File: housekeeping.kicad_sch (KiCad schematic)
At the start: 42 parts, among them U13 DAC53401, U15 MC34063A, U16 MC34063A

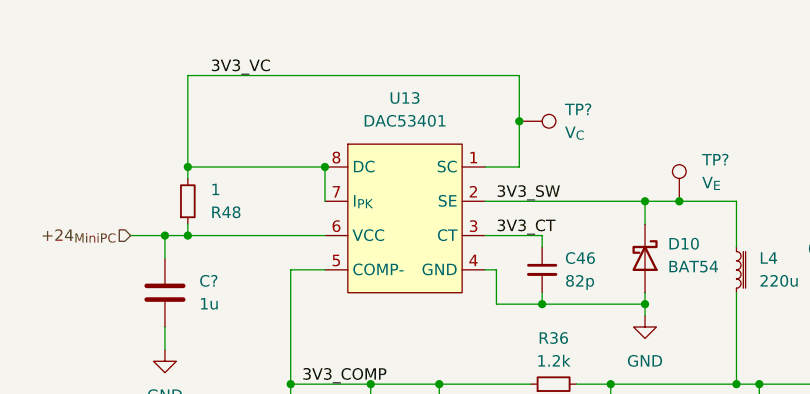
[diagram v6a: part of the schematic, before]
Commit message: Find suitable op-amp for buffer in current sense
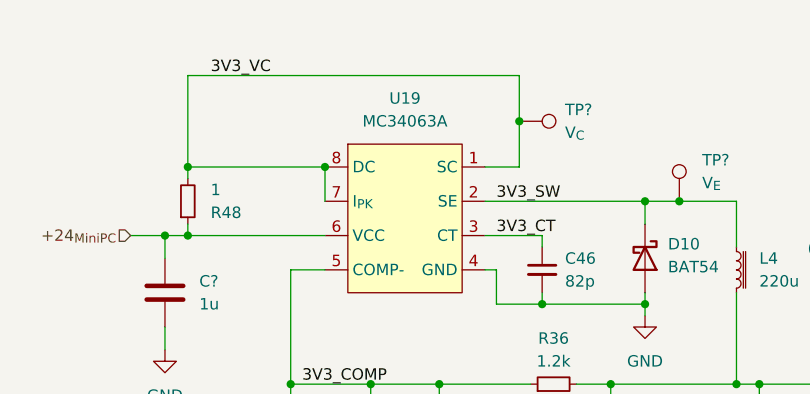
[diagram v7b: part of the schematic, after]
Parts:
- removed U13: DAC53401, Package_SON:WSON-8-1EP_2x2mm_P0.5mm_EP0.9x1.6mm, symbol ! Robomaster ICs:MC34063A
- added U19: MC34063A, Package_SO:SOIC-8_3.9x4.9mm_P1.27mm, symbol ! Robomaster ICs:MC34063A
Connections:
- net +24_{MiniPC}: now also U19.6 (VCC)
- net 3V3_COMP: now also U19.5 (COMP-)
- net 3V3_CT: now also U19.3 (CT)
- net 3V3_SW: now also U19.2 (SE)
- net 3V3_VC: now also U19.1 (SC), U19.7 (I_{PK}), U19.8 (DC)
- net GND: now also U19.4 (GND)
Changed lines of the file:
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@@
 	)
 	(junction
-		(at 68.58 46.99)
-		(diameter 0)
-		(color 0 0 0 0)
-	)
-	(junction
 		(at 217.17 72.39)
 		(diameter 0)
@@
 	)
 	(junction
+		(at 68.58 46.99)
+		(diameter 0)
+		(color 0 0 0 0)
+	)
+	(junction
 		(at 53.34 134.62)
 		(diameter 0)
@@
 	)
 	(symbol
-		(lib_id "! Robomaster ICs:MC34063A")
-		(at 77.47 44.45 0)
-		(unit 1)
-		(exclude_from_sim no)
-		(in_bom yes)
-		(on_board yes)
-		(dnp no)
-		(fields_autoplaced yes)
-		(property "Reference" "U13"
-			(at 77.47 39.37 0)
-			(effects
-				(font
-					(size 1.27 1.27)
-				)
-			)
-		)
-		(property "Value" "DAC53401"
-			(at 77.47 41.91 0)
-			(effects
-				(font
-					(size 1.27 1.27)
-				)
-			)
-		)
-		(property "Footprint" "Package_SON:WSON-8-1EP_2x2mm_P0.5mm_EP0.9x1.6mm"
-			(at 77.47 44.45 0)
-			(effects
-				(font
-					(size 1.27 1.27)
-				)
-				(hide yes)
-			)
-		)
-		(property "Datasheet" "https://www.ti.com/lit/gpn/mc34063a"
-			(at 77.47 44.45 0)
-			(effects
-				(font
-					(size 1.27 1.27)
-				)
-				(hide yes)
-			)
-		)
-		(property "Description" "1.5-A boost, buck, inverting switching regulator, operation from 0°C to 70°C"
-			(at 77.47 44.45 0)
-			(effects
-				(font
-					(size 1.27 1.27)
-				)
-				(hide yes)
-			)
-		)
-		(property "Mouser #" ""
-			(at 77.47 44.45 0)
-			(effects
-				(font
-					(size 1.27 1.27)
-				)
-				(hide yes)
-			)
-		)
-		(property "Mouser Link" ""
-			(at 77.47 44.45 0)
-			(effects
-				(font
-					(size 1.27 1.27)
-				)
-				(hide yes)
-			)
-		)
-		(property "JLCPCB #" ""
-			(at 77.47 44.45 0)
-			(effects
-				(font
-					(size 1.27 1.27)
-				)
-				(hide yes)
-			)
-		)
-		(property "Mouser Part Number" "595-DAC53401DSGR"
-			(at 77.47 44.45 0)
-			(effects
-				(font
-					(size 1.27 1.27)
-				)
-				(hide yes)
-			)
-		)
-		(property "Sim.Device" ""
-			(at 77.47 44.45 0)
-			(effects
-				(font
-					(size 1.27 1.27)
-				)
-			)
-		)
-		(property "Sim.Pins" ""
-			(at 77.47 44.45 0)
-			(effects
-				(font
-					(size 1.27 1.27)
-				)
-			)
-		)
-		(property "Sim.Type" ""
-			(at 77.47 44.45 0)
-			(effects
-				(font
-					(size 1.27 1.27)
-				)
-			)
-		)
-		(property "Height" ""
-			(at 77.47 44.45 0)
-			(effects
-				(font
-					(size 1.27 1.27)
-				)
-			)
-		)
-		(property "Manufacturer_Name" ""
-			(at 77.47 44.45 0)
-			(effects
-				(font
-					(size 1.27 1.27)
-				)
-			)
-		)
-		(property "Manufacturer_Part_Number" ""
-			(at 77.47 44.45 0)
-			(effects
-				(font
-					(size 1.27 1.27)
-				)
-			)
-		)
-		(property "Mouser Price/Stock" ""
-			(at 77.47 44.45 0)
-			(effects
-				(font
-					(size 1.27 1.27)
-				)
-			)
-		)
-		(pin "1"
-		)
-		(pin "4"
-		)
-		(pin "2"
-		)
-		(pin "6"
-		)
-		(pin "7"
-		)
-		(pin "3"
-		)
-		(pin "8"
-		)
-		(pin "5"
-		)
-		(instances
-			(project "SupercapManager"
-				(path "/6197145b-e7d4-44cc-9d90-537b6501bf60/2b4de7d2-e111-42d9-afee-f810f96a2f61"
-					(reference "U13")
-					(unit 1)
-				)
-			)
-			(project "Housekeeping Rev1"
-				(path "/d2a5f610-b666-4f42-b17a-f8b6e55a52c2/25bdba42-617b-4aa1-85da-258c1454f7e3"
-					(reference "U1")
-					(unit 1)
-				)
-			)
-		)
-	)
-	(symbol
 		(lib_id "Connector:TestPoint")
 		(at 90.17 121.92 270)
@@
 					(unit 1)
 				)
+			)
+		)
+	)
+	(symbol
+		(lib_id "! Robomaster ICs:MC34063A")
+		(at 77.47 44.45 0)
+		(unit 1)
+		(exclude_from_sim no)
+		(in_bom yes)
+		(on_board yes)
+		(dnp no)
+		(fields_autoplaced yes)
+		(property "Reference" "U19"
+			(at 77.47 39.37 0)
+			(effects
+				(font
+					(size 1.27 1.27)
+				)
+			)
+		)
+		(property "Value" "MC34063A"
+			(at 77.47 41.91 0)
+			(effects
+				(font
+					(size 1.27 1.27)
+				)
+			)
+		)
+		(property "Footprint" "Package_SO:SOIC-8_3.9x4.9mm_P1.27mm"
+			(at 77.47 44.45 0)
+			(effects
+				(font
+					(size 1.27 1.27)
+				)
+				(hide yes)
+			)
+		)
+		(property "Datasheet" "https://www.ti.com/lit/gpn/mc34063a"
+			(at 77.47 44.45 0)
+			(effects
+				(font
+					(size 1.27 1.27)
+				)
+				(hide yes)
+			)
+		)
+		(property "Description" "1.5-A boost, buck, inverting switching regulator, operation from 0°C to 70°C"
+			(at 77.47 44.45 0)
+			(effects
+				(font
+					(size 1.27 1.27)
+				)
+				(hide yes)
+			)
+		)
+		(property "Mouser #" ""
+			(at 77.47 44.45 0)
+			(effects
+				(font
+					(size 1.27 1.27)
+				)
+				(hide yes)
+			)
+		)
+		(property "Mouser Link" ""
+			(at 77.47 44.45 0)
+			(effects
+				(font
+					(size 1.27 1.27)
+				)
+				(hide yes)
+			)
+		)
+		(property "JLCPCB #" ""
+			(at 77.47 44.45 0)
+			(effects
+				(font
+					(size 1.27 1.27)
+				)
+				(hide yes)
+			)
+		)
+		(property "Mouser Part Number" "595-MC34063ADR"
+			(at 77.47 44.45 0)
+			(effects
+				(font
+					(size 1.27 1.27)
+				)
+				(hide yes)
+			)
+		)
+		(property "Sim.Device" ""
+			(at 77.47 44.45 0)
+			(effects
+				(font
+					(size 1.27 1.27)
+				)
+			)
+		)
+		(property "Sim.Pins" ""
+			(at 77.47 44.45 0)
+			(effects
+				(font
+					(size 1.27 1.27)
+				)
+			)
+		)
+		(property "Sim.Type" ""
+			(at 77.47 44.45 0)
+			(effects
+				(font
+					(size 1.27 1.27)
+				)
+			)
+		)
+		(property "Height" ""
+			(at 77.47 44.45 0)
+			(effects
+				(font
+					(size 1.27 1.27)
+				)
+			)
+		)
+		(property "Manufacturer_Name" ""
+			(at 77.47 44.45 0)
+			(effects
+				(font
+					(size 1.27 1.27)
+				)
+			)
+		)
+		(property "Manufacturer_Part_Number" ""
+			(at 77.47 44.45 0)
+			(effects
+				(font
+					(size 1.27 1.27)
+				)
+			)
+		)
+		(property "Mouser Price/Stock" ""
+			(at 77.47 44.45 0)
+			(effects
+				(font
+					(size 1.27 1.27)
+				)
+			)
+		)
+		(pin "1"
+		)
+		(pin "4"
+		)
+		(pin "2"
+		)
+		(pin "6"
+		)
+		(pin "7"
+		)
+		(pin "3"
+		)
+		(pin "8"
+		)
+		(pin "5"
+		)
+		(instances
+			(project "SupercapManager"
+				(path "/6197145b-e7d4-44cc-9d90-537b6501bf60/2b4de7d2-e111-42d9-afee-f810f96a2f61"
+					(reference "U19")
+					(unit 1)
+				)
